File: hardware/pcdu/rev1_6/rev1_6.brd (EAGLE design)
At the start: 90 x 16.2 mm, 17 parts, among them IC1 74HC595N, X1 MUSBV, X2 MUSBV, X3 MUSBV, X4 MUSBV, X7 22-23-2041, X8 22-23-2041

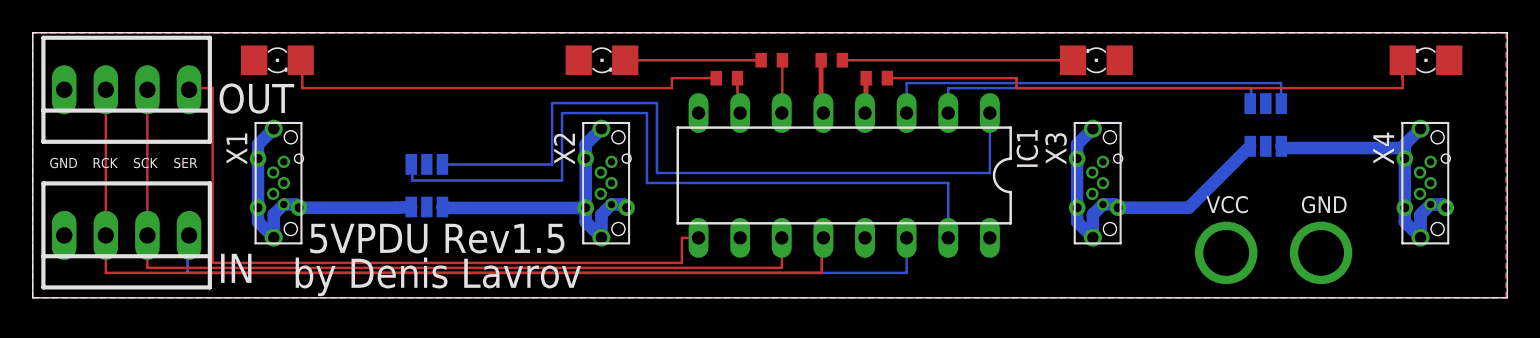
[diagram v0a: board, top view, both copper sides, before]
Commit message: Updated PDU board, removed screw terminal
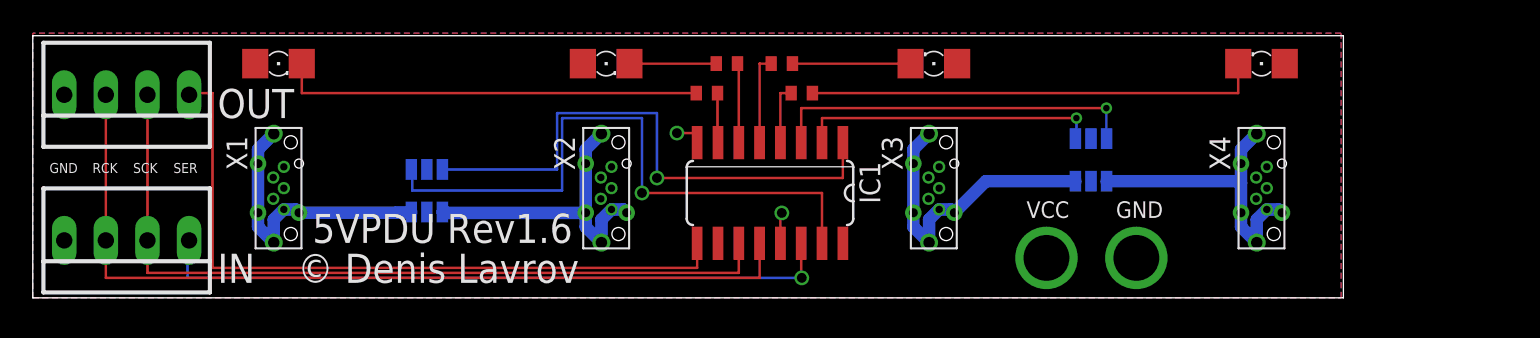
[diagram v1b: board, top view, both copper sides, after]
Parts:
- IC1: value 74HC595N -> 74HC595D; device 74xx-eu:DIL16 -> 74xx-eu:SO16
- moved U$2 10.9 mm to (63.1, 7.52)
- moved LED4 10.0 mm to (75.0, 14.3)
- moved X3 10.0 mm to (55.0, 6.70)
- moved X4 10.0 mm to (75.0, 6.70)
- moved LED3 9.92 mm to (55.0, 14.3)
- moved R1 4.66 mm to (46.9, 12.5)
- moved IC1 4.65 mm to (45.0, 6.40)
- moved R2 3.05 mm to (45.7, 14.3)
- moved R3 2.75 mm to (42.4, 14.3)
- moved R4 1.52 mm to (41.1, 12.5)
- moved LED2 0.33 mm to (35.0, 14.3)
- moved U$1 0.30 mm to (22.6, 5.64)
- moved X1 0.30 mm to (15.0, 6.70)
- moved X2 0.30 mm to (35.0, 6.70)
- moved X7 0.30 mm to (5.73, 3.51)
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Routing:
- net N$2: track 45.1 -> 34.0 mm, vias 0 -> 1
- net N$1: track 45.4 -> 38.4 mm, vias 0 -> 1
- net N$5: track 34.9 -> 27.8 mm
- net N$6: track 14.1 -> 7.21 mm
- net SIN: track 48.4 -> 42.0 mm, vias 0 -> 1
- net RCK: track 57.1 -> 53.2 mm
- net GND: track 0.00 -> 3.76 mm, vias 1 -> 3
- net N$4: track 26.0 -> 22.6 mm, vias 0 -> 1
- net N$7: track 8.29 -> 5.30 mm
- net N$3: track 21.0 -> 18.3 mm, vias 0 -> 1
- net SCK: track 51.4 -> 48.8 mm
- net N$14: track 3.36 -> 5.53 mm
- net N$8: track 28.0 -> 25.9 mm
- net N$15: track 3.26 -> 4.85 mm
- net N$13: track 2.13 -> 3.68 mm
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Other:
- board size 90 x 16.2 mm -> 80 x 16 mm
- board text added: "5VPDU Rev1.6"
- board text added: "© Denis Lavrov"
- board text removed: "5VPDU Rev1.5"
- board text removed: "by Denis Lavrov"

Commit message: Added new mounting desing for RPi
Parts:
- moved X7 8.84 mm to (5.43, 12.3)
- moved X8 8.54 mm to (5.43, 3.86)
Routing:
- net SIN: track 42.0 -> 51.0 mm
- net SOUT: track 43.3 -> 34.9 mm
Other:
- board text added: "Direction of Board"
- board text added: "ETH+USB"
- board text added: "SD Card"
